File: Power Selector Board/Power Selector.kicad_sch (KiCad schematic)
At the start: 3 parts, among them J101 MSD-DB01M-12P, J102 MSD-DB01F-12P_1, U101 1720466

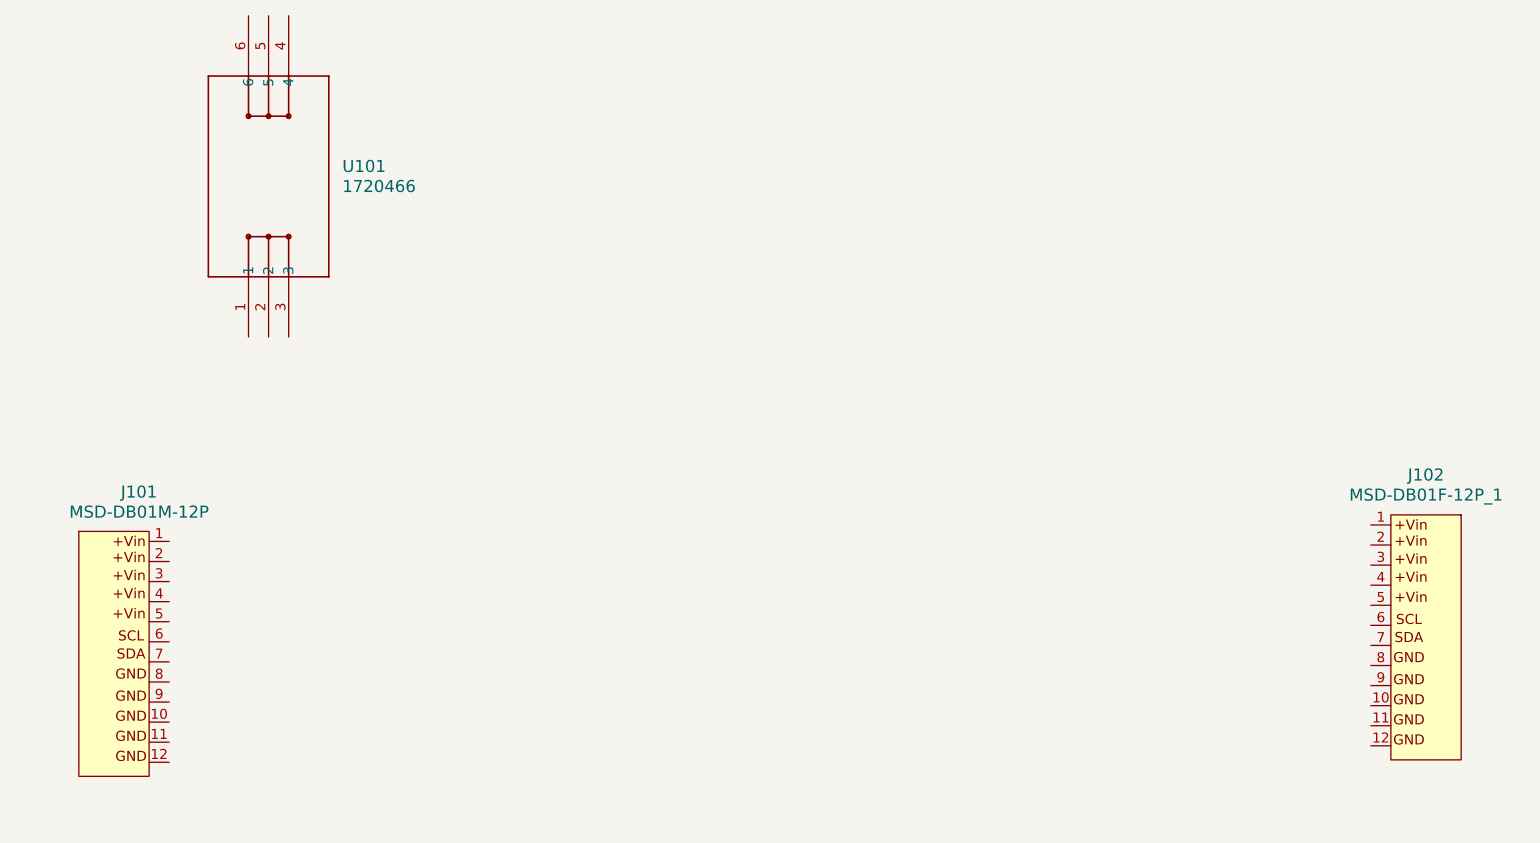
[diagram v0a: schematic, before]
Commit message: Changements mineurs aux connections des connecteurs
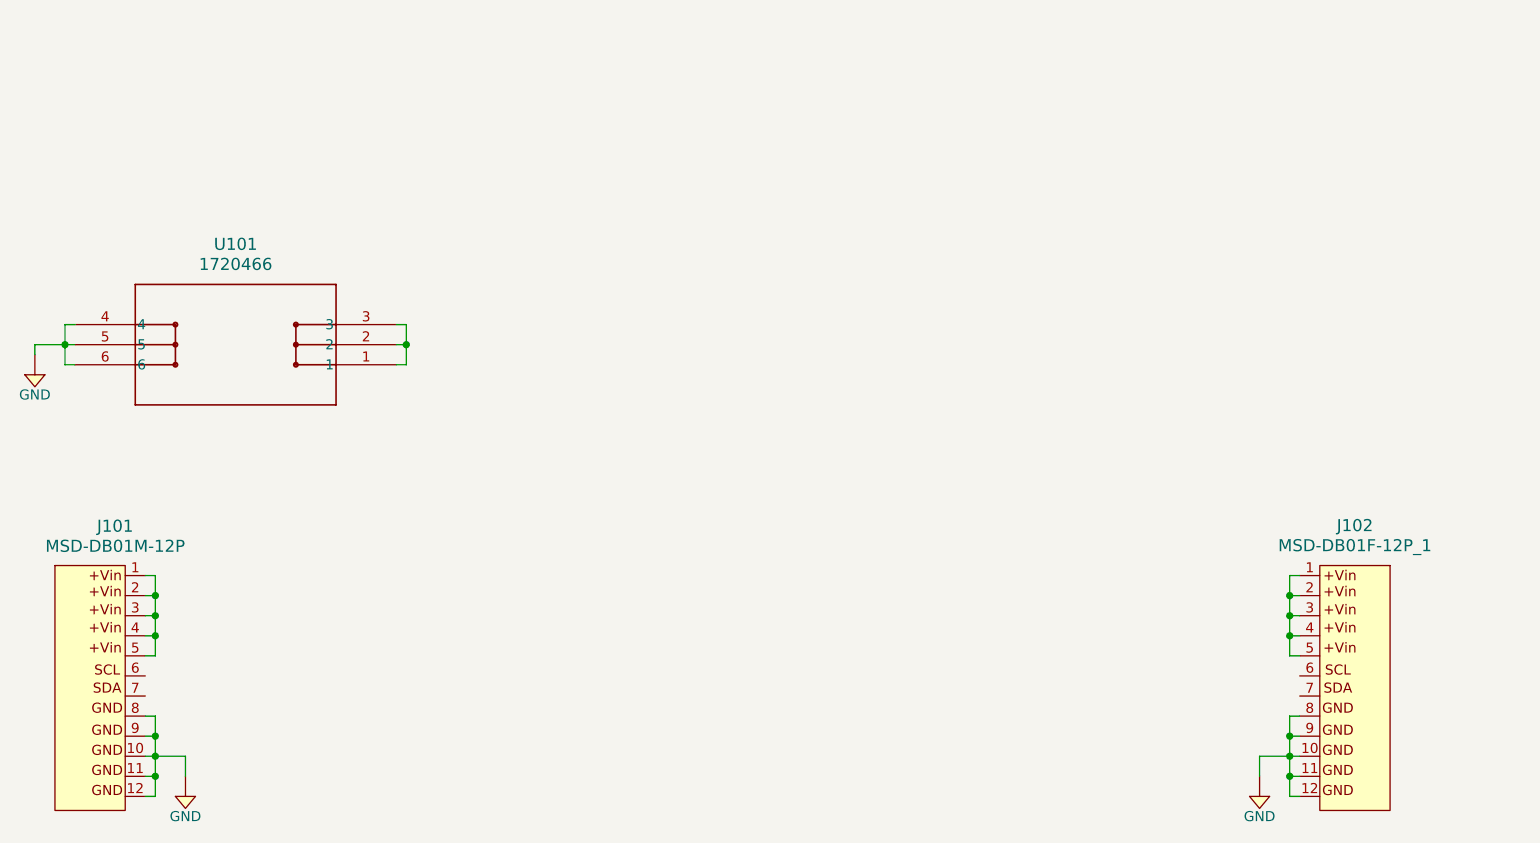
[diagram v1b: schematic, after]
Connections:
- net at J102.1: now also J102.2, J102.3, J102.4, J102.5
- net GND: now reaches J102.10
- net GND: now also J101.10, J101.11, J101.12, J101.8, J101.9, J102.11, J102.12, J102.8, J102.9, U101.4, U101.5, U101.6
- net at J101.1: now also J101.2, J101.3, J101.4, J101.5
- net at U101.1: now also U101.2, U101.3
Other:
- moved on the sheet: J101, J102, U101

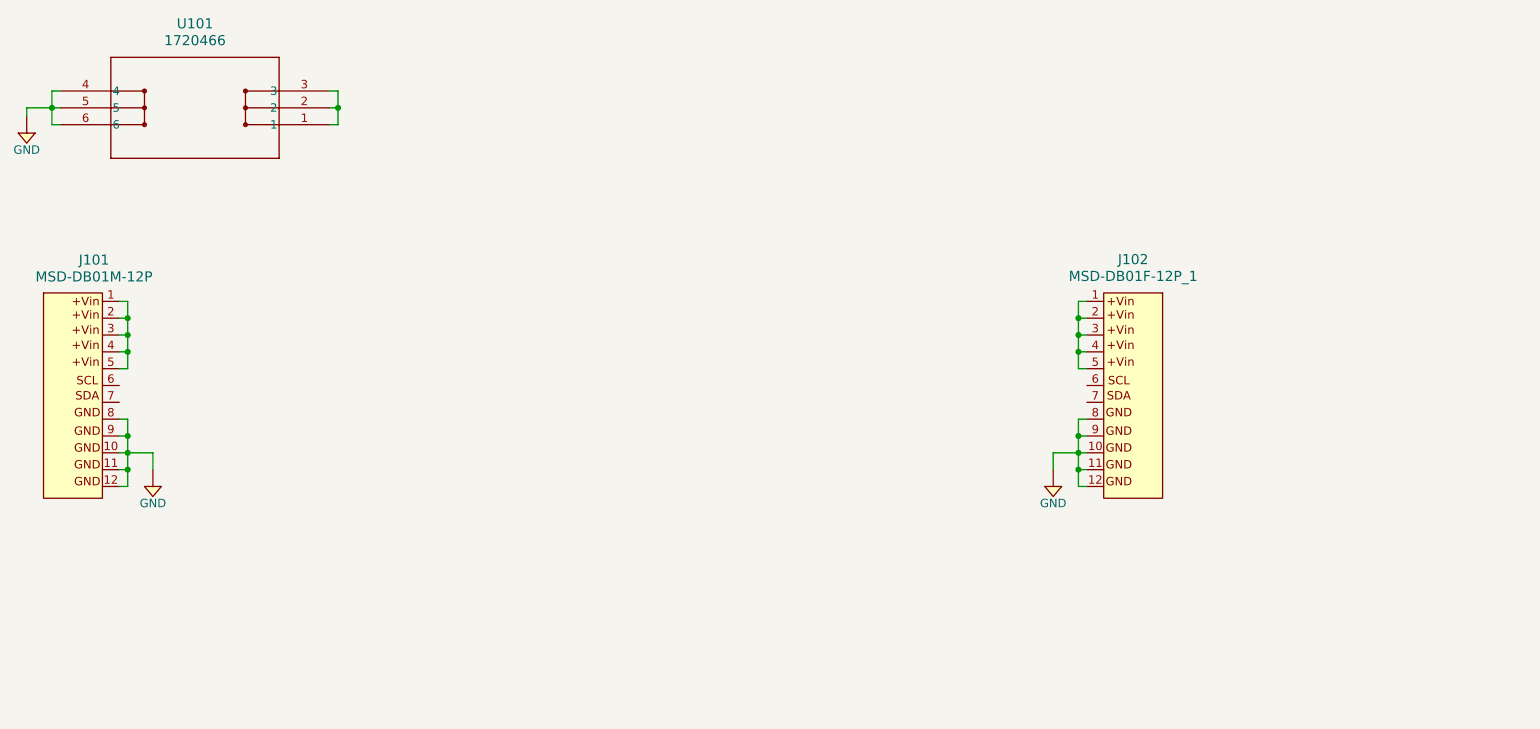
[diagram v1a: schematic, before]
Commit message: Ajout d'un relais et completion du circuit de controle
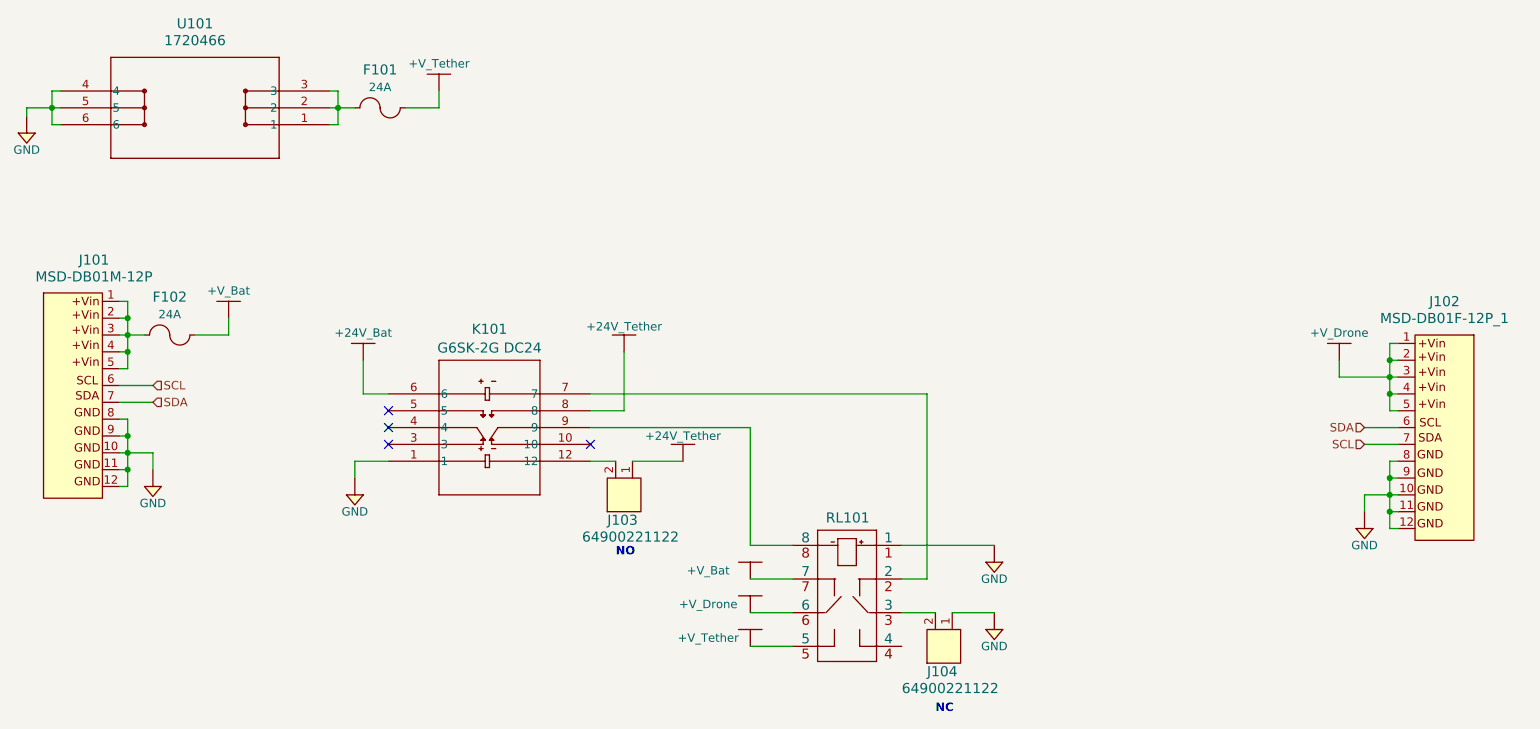
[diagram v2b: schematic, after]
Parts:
- added F101, F102: 047706.3MRET1P, Fuses:3587TR, symbol Fuses:047706.3MRET1P
- added J103, J104: 64900221122, Connectors:64900221122, symbol Connectors:64900221122
- added K101: G6SK-2G DC24, Relays:G6SK-2G DC3_OMR, symbol Relays:G6SK-2G_DC24
- added RL101: 2-1462039-9, Relays:2-1462039-9, symbol Relays:2-1462039-9
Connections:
- net GND: now also J104.1, K101.1, RL101.1
- net +VBat: now reaches J102.1, J102.2, J102.3, J102.4, J102.5
- net +VBat: now also F101.~, F102.~, RL101.5, RL101.6, RL101.7
- net SDA: now reaches J102.6
- net SDA: now also J101.7
- net SCL: now reaches J102.7
- net SCL: now also J101.6
- net at J101.1, J101.2, J101.3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: now also F102.~
- net at U101.1, U101.2, U101.3: now also F101.~
- new net: J103.2, K101.12
- new net: K101.7, RL101.2
- new net: K101.9, RL101.8
- new net: J104.2, RL101.3
- new net 24V: J103.1, K101.6, K101.8
- no-connect marks 0 -> 4
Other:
- note added: "NC"
- note added: "NO"
- moved on the sheet: J102

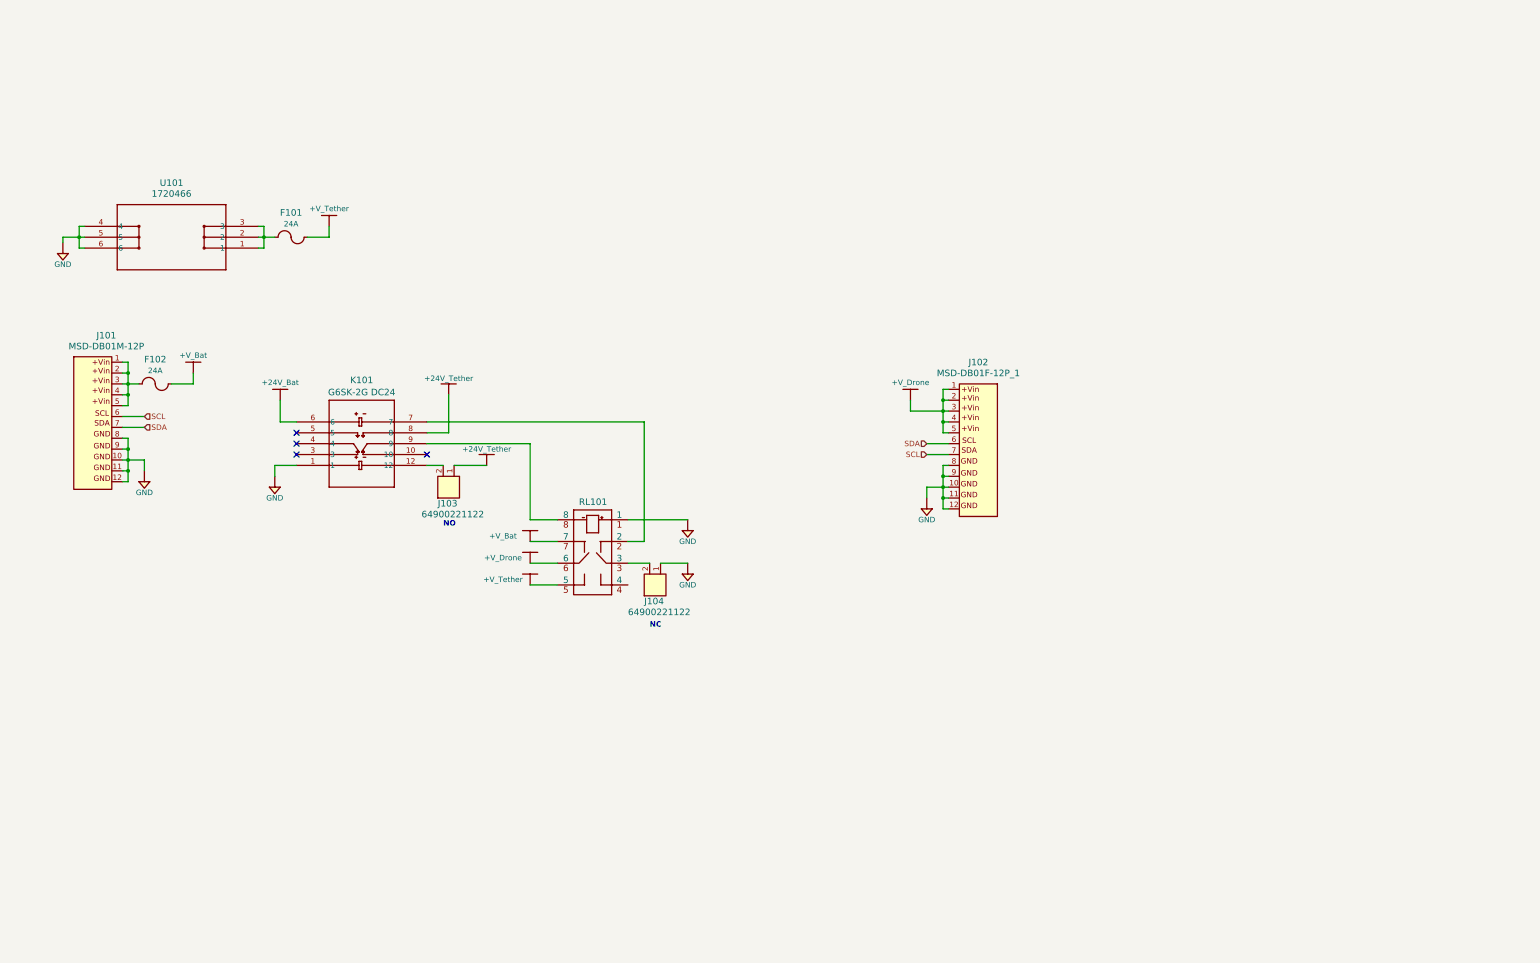
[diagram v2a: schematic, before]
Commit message: Clarification de la schematic, ajout de commentaires
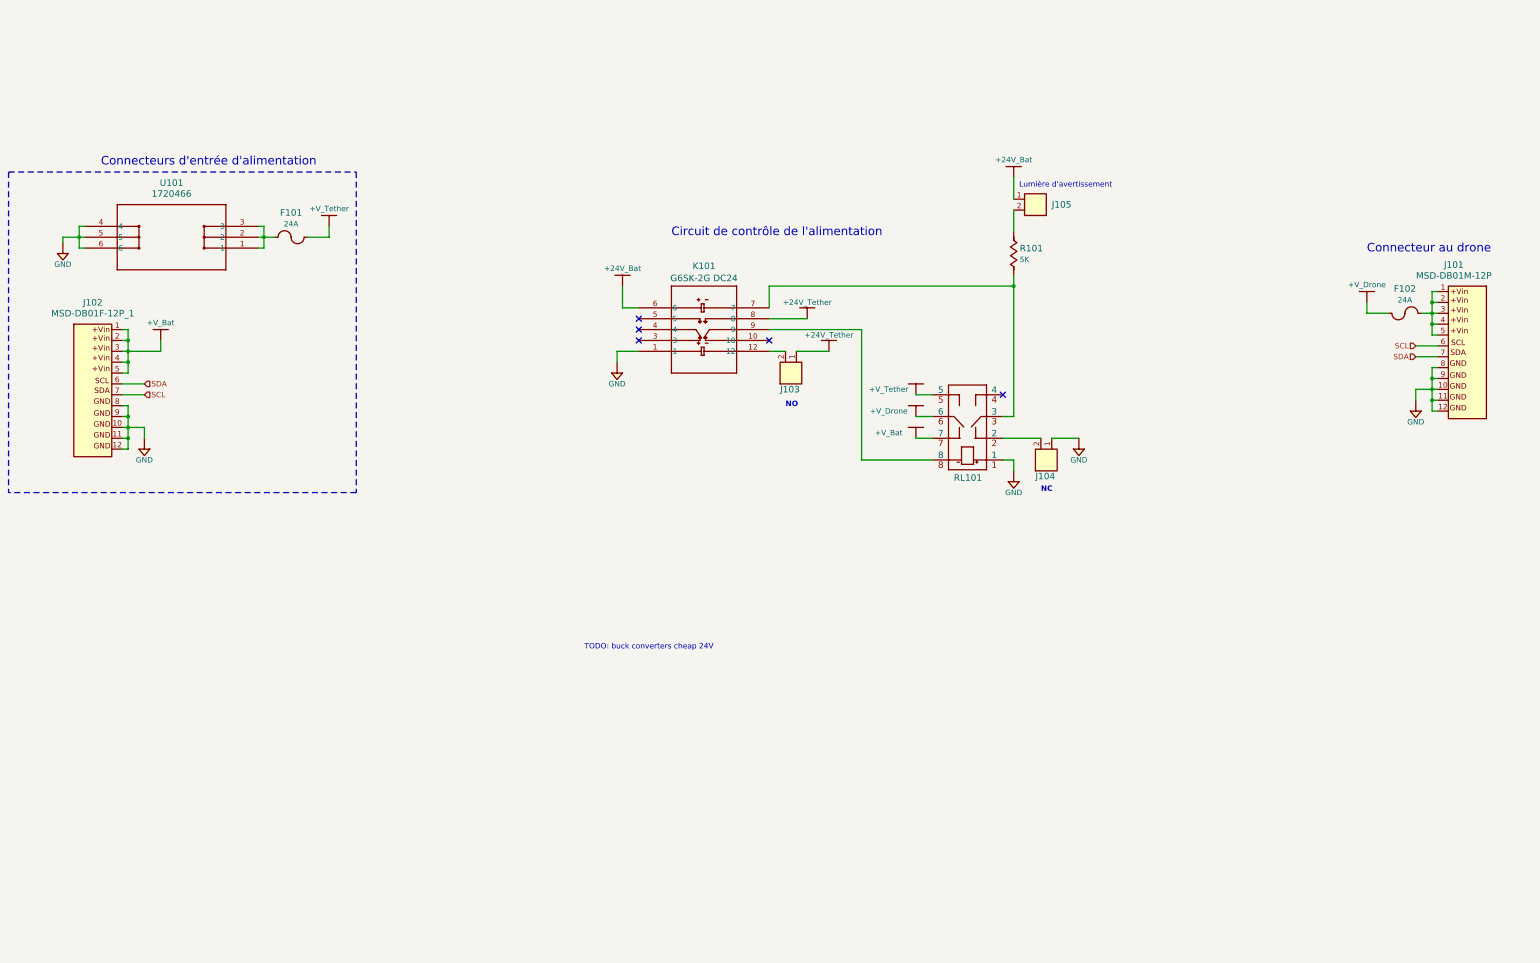
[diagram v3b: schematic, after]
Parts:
- added J105: 64900221122, Connectors:64900221122, symbol Connectors:64900221122
- added R101: RC1206JR-07120RL, Resistors:R1206, symbol Resistors:RC1206JR-07120RL
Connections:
- net 24V: now also J105.1
- net at K101.7: now also RL101.3, R101.1; no longer RL101.2
- net at J104.2: now also RL101.2; no longer RL101.3
- new net: J105.2, R101.2
- no-connect marks 4 -> 5
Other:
- note added: "Circuit de contrôle de l'alimentation"
- note added: "Connecteur au drone"
- note added: "Connecteurs d'entrée d'alimentation"
- note added: "Lumière d'avertissement"
- note added: "TODO: buck converters cheap 24V"
- moved on the sheet: J102, J103, J104, K101, RL101
